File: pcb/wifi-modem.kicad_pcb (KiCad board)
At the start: 2 copper layers, 102.5 x 66.1 mm, 36 parts, among them J1 UART1 3V3 TTL, J2 RS232 DB9, J3 5.5X2.1MM, U1 74HC245, U2 WeMos_D1_mini, U3 MAX232, U4 SN74HC08N

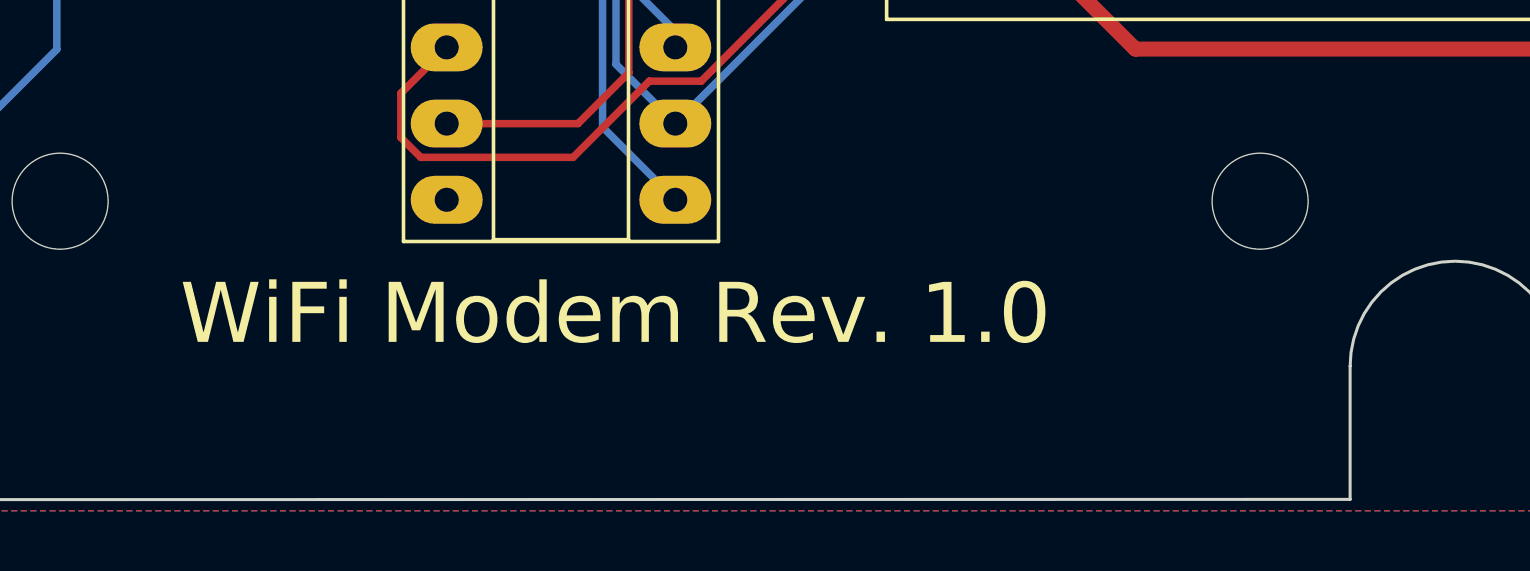
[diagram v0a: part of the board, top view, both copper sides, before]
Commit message: Rev 1.1
* Cleaning up schematic
* Adding missing copper void
* Added net names for RS232 signals
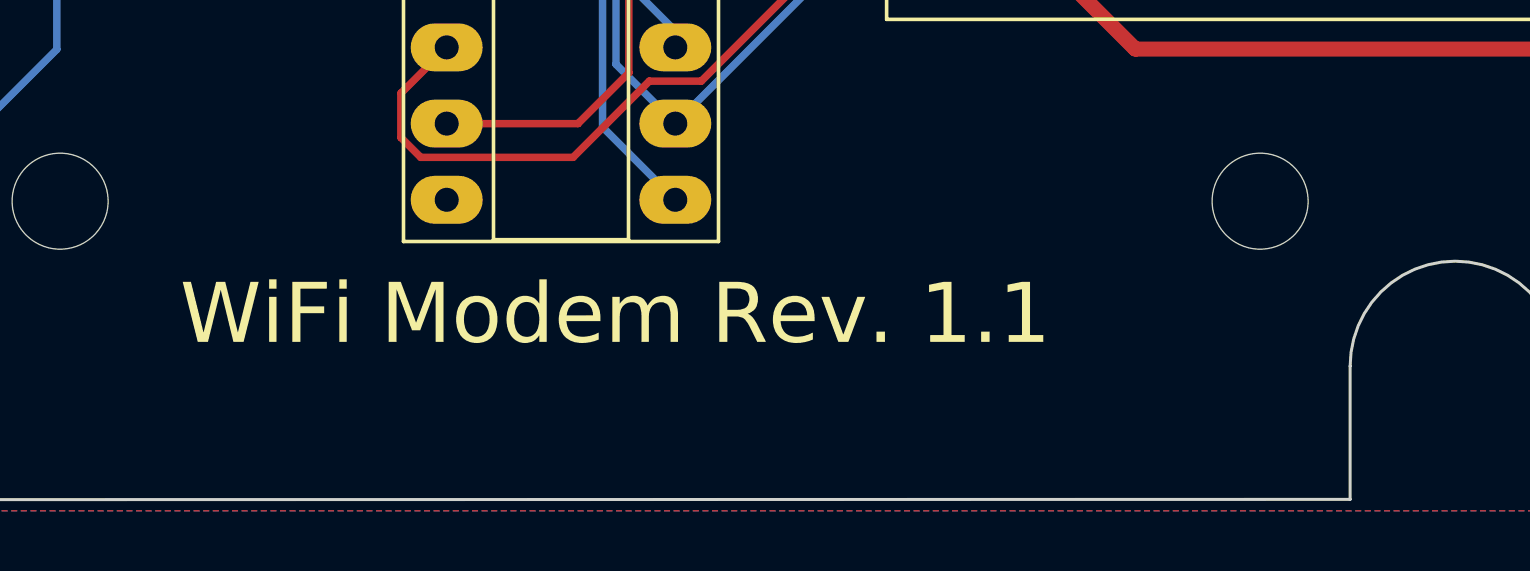
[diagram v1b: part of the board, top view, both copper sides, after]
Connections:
- net Net-(J2-Pad2) renamed /RS232_RXD
- net Net-(J2-Pad3) renamed /RS232_TXD
- net Net-(J2-Pad7) renamed /RS232_RTS
- net Net-(J2-Pad8) renamed /RS232_CTS
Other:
- board text added: "WiFi Modem Rev. 1.1"
- board text removed: "WiFi Modem Rev. 1.0"

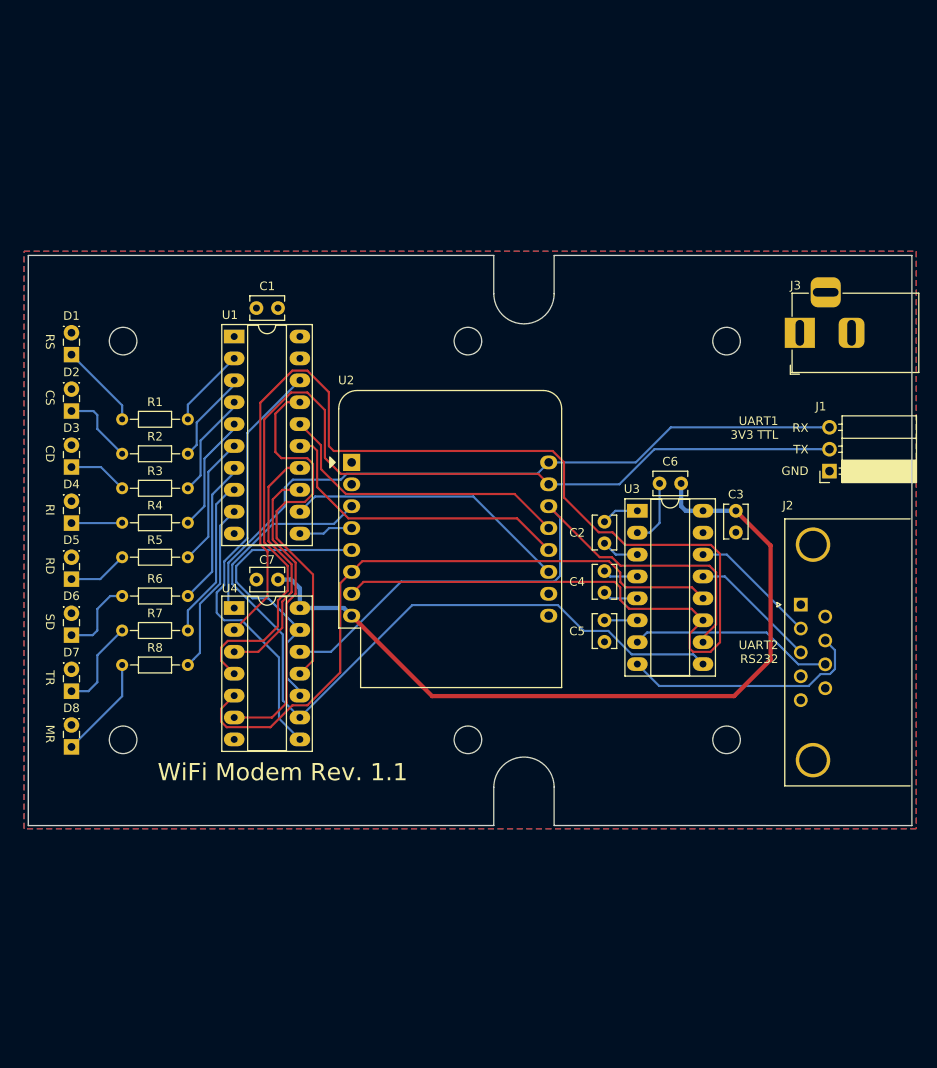
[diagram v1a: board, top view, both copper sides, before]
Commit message: PCB layout + footprint changes
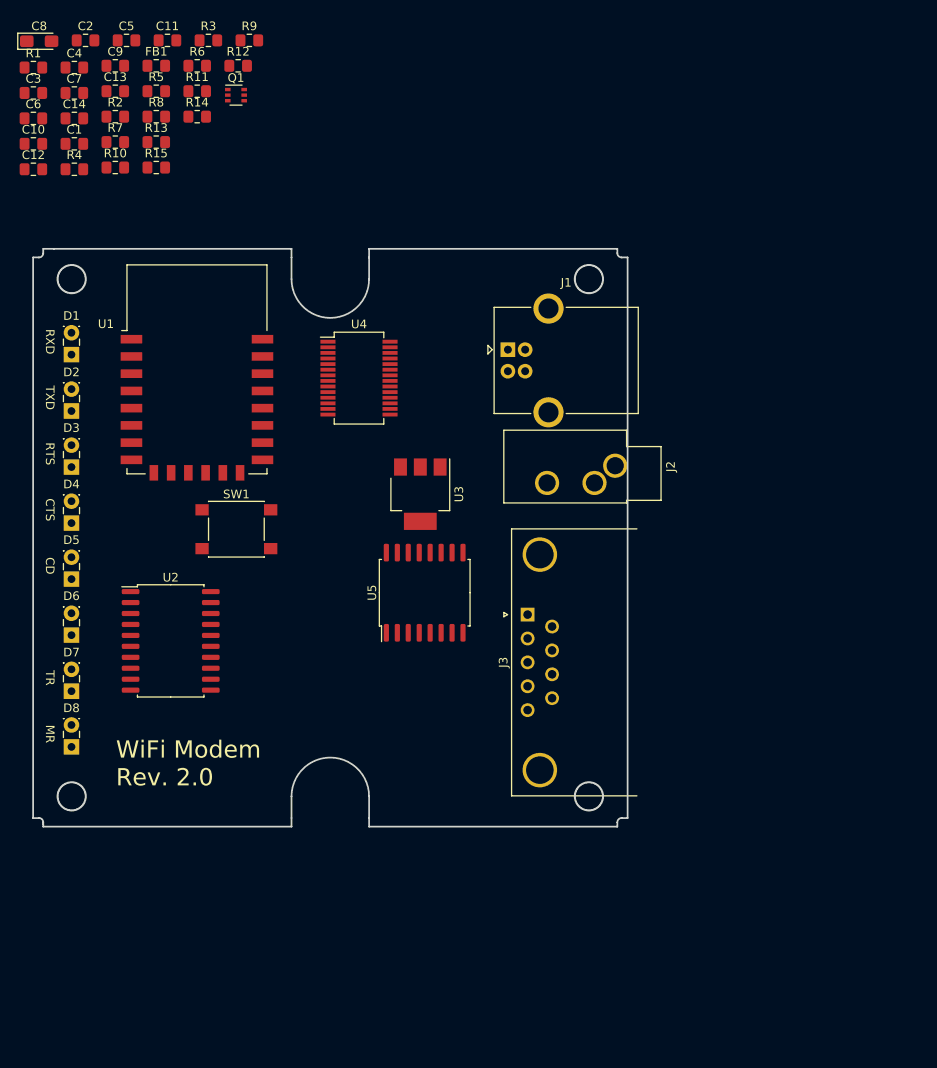
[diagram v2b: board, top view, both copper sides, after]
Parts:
- removed H5, H6: MountingHole, MountingHole:MountingHole_3.2mm_M3
- added C10: 100n, Capacitor_SMD:C_0805_2012Metric_Pad1.15x1.40mm_HandSolder, F.Cu at (38.7, 50.5)
- added C11: 100n, Capacitor_SMD:C_0805_2012Metric_Pad1.15x1.40mm_HandSolder, F.Cu at (54.2, 38.5)
- added C12: 100n, Capacitor_SMD:C_0805_2012Metric_Pad1.15x1.40mm_HandSolder, F.Cu at (38.7, 53.5)
- added C13: 100n, Capacitor_SMD:C_0805_2012Metric_Pad1.15x1.40mm_HandSolder, F.Cu at (48.2, 44.4)
- added C14: 10n, Capacitor_SMD:C_0805_2012Metric_Pad1.15x1.40mm_HandSolder, F.Cu at (43.4, 47.6)
- added C8: 4.7u, Capacitor_Tantalum_SMD:CP_EIA-3216-18_Kemet-A_Pad1.58x1.35mm_HandSolder, F.Cu at (39.4, 38.6)
- added C9: 100n, Capacitor_SMD:C_0805_2012Metric_Pad1.15x1.40mm_HandSolder, F.Cu at (48.2, 41.5)
- added FB1: 33 Ohms @ 100MHz, Inductor_SMD:L_0805_2012Metric_Pad1.15x1.40mm_HandSolder, F.Cu at (52.9, 41.5)
- added Q1: BC846BDW1, Package_TO_SOT_SMD:SOT-363_SC-70-6, F.Cu at (62.2, 44.9)
- added R10: 560, Resistor_SMD:R_0805_2012Metric_Pad1.15x1.40mm_HandSolder, F.Cu at (48.2, 53.3)
- added R11: 560, Resistor_SMD:R_0805_2012Metric_Pad1.15x1.40mm_HandSolder, F.Cu at (57.7, 44.4)
- added R12: 10k, Resistor_SMD:R_0805_2012Metric_Pad1.15x1.40mm_HandSolder, F.Cu at (62.4, 41.5)
- added R13: 10k, Resistor_SMD:R_0805_2012Metric_Pad1.15x1.40mm_HandSolder, F.Cu at (52.9, 50.3)
- added R14: 10k, Resistor_SMD:R_0805_2012Metric_Pad1.15x1.40mm_HandSolder, F.Cu at (57.7, 47.4)
- added R15: 10k, Resistor_SMD:R_0805_2012Metric_Pad1.15x1.40mm_HandSolder, F.Cu at (52.9, 53.3)
- added R9: 560, Resistor_SMD:R_0805_2012Metric_Pad1.15x1.40mm_HandSolder, F.Cu at (63.7, 38.5)
- added SW1: SW_Push, Button_Switch_SMD:SW_SPST_PTS645, F.Cu at (62.2, 95.2)
- added U5: MAX232, Package_SO:SOIC-16W_7.5x10.3mm_P1.27mm, F.Cu at (84.1, 102.6)
- C1, C2, C5, C6, C7: footprint Capacitor_THT:C_Disc_D3.8mm_W2.6mm_P2.50mm -> Capacitor_SMD:C_0805_2012Metric_Pad1.15x1.40mm_HandSolder
- C3: value 100n -> 100u; footprint Capacitor_THT:C_Disc_D3.8mm_W2.6mm_P2.50mm -> Capacitor_SMD:C_0805_2012Metric_Pad1.15x1.40mm_HandSolder
- C4: value 100n -> 10u; footprint Capacitor_THT:C_Disc_D3.8mm_W2.6mm_P2.50mm -> Capacitor_SMD:C_0805_2012Metric_Pad1.15x1.40mm_HandSolder
- D1: value RS (Request to Send) -> LED
- D2: value CS (Clear to Send) -> LED
- D3: value CD (Data Carrier Detect) -> LED
- D4: value RI (Ring) -> LED
- D5: value RD (Receive Data) -> LED
- D6: value SD (Send Data) -> LED
- D7: value TR (Terminal Ready) -> LED
- D8: value MR (Modem Ready) -> LED
- J1: value UART1 3V3 TTL -> USB_B; footprint Connector_PinSocket_2.54mm:PinSocket_1x03_P2.54mm_Horizontal -> Connector_USB:USB_B_OST_USB-B1HSxx_Horizontal
- J2: value RS232 DB9 -> AudioJack3; footprint Connector_Dsub:DSUB-9_Female_Horizontal_P2.77x2.84mm_EdgePinOffset9.90mm_Housed_MountingHolesOffset11.32mm -> Connector_Audio:Jack_3.5mm_CUI_SJ1-3533NG_Horizontal_CircularHoles
- J3: value 5.5X2.1MM -> RS232 DB9; footprint Connector_BarrelJack:BarrelJack_Horizontal -> Connector_Dsub:DSUB-9_Female_Horizontal_P2.77x2.84mm_EdgePinOffset9.90mm_Housed_MountingHolesOffset11.32mm
- R1, R2, R3: value 560 -> 10k; footprint Resistor_THT:R_Axial_DIN0204_L3.6mm_D1.6mm_P7.62mm_Horizontal -> Resistor_SMD:R_0805_2012Metric_Pad1.15x1.40mm_HandSolder
- R4, R5, R6, R7, R8: footprint Resistor_THT:R_Axial_DIN0204_L3.6mm_D1.6mm_P7.62mm_Horizontal -> Resistor_SMD:R_0805_2012Metric_Pad1.15x1.40mm_HandSolder
- U1: value 74HC245 -> ESP-12F; footprint Package_DIP:DIP-20_W7.62mm_Socket_LongPads -> RF_Module:ESP-12E
- U2: value WeMos_D1_mini -> 74HC245; footprint Module:WEMOS_D1_mini_light -> Package_SO:SOIC-20W_7.5x12.8mm_P1.27mm
- U3: value MAX232 -> LM1117-3.3; footprint Package_DIP:DIP-16_W7.62mm_Socket_LongPads -> Package_TO_SOT_SMD:SOT-223-3_TabPin2
- U4: value SN74HC08N -> FT232RL; footprint Package_DIP:DIP-14_W7.62mm_Socket_LongPads -> Package_SO:SSOP-28_5.3x10.2mm_P0.65mm
- moved C3 94.8 mm to (38.7, 44.6), turned to 0 degrees
- moved C5 87.2 mm to (49.5, 38.5), turned to 0 degrees
- moved C6 86.2 mm to (38.7, 47.6), turned to 0 degrees
- moved C4 84.8 mm to (43.4, 41.7), turned to 0 degrees
- moved C2 82.1 mm to (44.7, 38.5), turned to 0 degrees
- moved H2 76.0 mm to (103.1, 66.2)
- moved H3 70.0 mm to (43.1, 126.2)
- moved R8 63.7 mm to (52.9, 47.4), turned to 0 degrees
- moved R6 61.5 mm to (57.7, 41.5), turned to 0 degrees
- moved C7 61.2 mm to (43.4, 44.6), turned to 0 degrees
- moved R7 57.3 mm to (48.2, 50.3), turned to 0 degrees
- moved R5 54.2 mm to (52.9, 44.4), turned to 0 degrees
- moved R3 52.0 mm to (59.0, 38.5), turned to 0 degrees
- moved J3 45.4 mm to (96.0, 105.2), turned to 90 degrees
- moved R1 44.6 mm to (38.7, 41.7), turned to 0 degrees
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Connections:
- C2 pad 1: Net-(C2-Pad1) -> +3V3
- C2 pad 2: Net-(C2-Pad2) -> GND
- C4 pad 1: Net-(C4-Pad1) -> +5V
- C4 pad 2: Net-(C4-Pad2) -> GND
- C5 pad 1: Net-(C5-Pad1) -> +5V
- C6 pad 1: +3V3 -> Net-(C6-Pad1)
- J1 pad 1: GND -> VBUS
- J1 pad 2: TX1 -> Net-(J1-Pad2)
- J1 pad 3: RX1 -> Net-(J1-Pad3)
- J3 pad 1: +5V -> (no net)
- J3 pad 2: GND -> RS232_TXD
- J3 pad 3: Net-(J3-Pad3) -> RS232_RXD
- R1 pad 1: Net-(R1-Pad1) -> +3V3
- R1 pad 2: Net-(D1-Pad1) -> ESP_GPIO2
- R2 pad 1: Net-(R2-Pad1) -> +3V3
- R2 pad 2: Net-(D2-Pad1) -> ESP_GPIO0
- R3 pad 1: Net-(R3-Pad1) -> +3V3
- R3 pad 2: Net-(D3-Pad1) -> ESP_RST_N
- R4 pad 1: Net-(R4-Pad1) -> RX_LED_DRV
- R4 pad 2: Net-(D4-Pad1) -> Net-(D1-Pad1)
- R5 pad 1: Net-(R5-Pad1) -> TX_LED_DRV
- R5 pad 2: Net-(D5-Pad1) -> Net-(D2-Pad1)
- R6 pad 1: Net-(R6-Pad1) -> RTS_LED_DRV
- R6 pad 2: Net-(D6-Pad1) -> Net-(D3-Pad1)
- R7 pad 1: Net-(R7-Pad1) -> CTS_LED_DRV
- R7 pad 2: Net-(D7-Pad1) -> Net-(D4-Pad1)
- R8 pad 1: Net-(R8-Pad1) -> CD_LED_DRV
- R8 pad 2: Net-(D8-Pad1) -> Net-(D5-Pad1)
- U1 pad 1: GND -> ESP_RST_N
- U1 pad 10: GND -> (no net)
- U1 pad 11: MR -> (no net)
- U1 pad 12: TR -> (no net)
- U1 pad 13: TX_LED -> (no net)
- U1 pad 14: RX_LED -> (no net)
- U1 pad 15: RI -> GND
- U1 pad 16: CD -> ESP_GPIO15_UART0_RTS
- U1 pad 17: CS_LED -> ESP_GPIO2
- U1 pad 18: RS_LED -> ESP_GPIO0
- U1 pad 19: GND -> ESP_GPIO4
- U1 pad 2: Net-(R1-Pad1) -> (no net)
- U1 pad 20: +5V -> ESP_GPIO5
- U1 pad 3: Net-(R2-Pad1) -> ESP_EN
- U1 pad 4: Net-(R3-Pad1) -> (no net)
- U1 pad 5: Net-(R4-Pad1) -> ESP_GPIO14
- U1 pad 6: Net-(R5-Pad1) -> ESP_GPIO12
- U1 pad 7: Net-(R6-Pad1) -> ESP_UART0_CTS
- U1 pad 8: Net-(R7-Pad1) -> +3V3
- U1 pad 9: Net-(R8-Pad1) -> (no net)
- U2 pad 1: Net-(U2-Pad1) -> GND
- U2 pad 11: TR -> ESP_GPIO14
- U2 pad 12: RI -> ESP_GPIO12
- U2 pad 13: CD -> ESP_GPIO5
- U2 pad 14: CS -> ESP_GPIO4
- U2 pad 15: TX1 -> ESP_GPIO15_UART0_RTS
- U2 pad 16: RX1 -> ESP_UART0_CTS
- U2 pad 2: Net-(U2-Pad2) -> RX_LED_DRV
- U2 pad 3: RS -> TX_LED_DRV
- U2 pad 4: MR -> RTS_LED_DRV
- U2 pad 5: HS_DISP_CTRL -> CTS_LED_DRV
- U2 pad 6: TX2 -> CD_LED_DRV
- U2 pad 7: RX2 -> RI_LED_DRV
- U2 pad 8: +3V3 -> TR_LED_DRV
- U2 pad 9: +5V -> MR_LED_DRV
- U3 pad 1: Net-(C2-Pad1) -> GND
- U3 pad 2: Net-(C6-Pad2) -> +3V3
- U3 pad 3: Net-(C2-Pad2) -> +5V
- U4 pad 1: RX1 -> 3V3_TTL_RXD
- U4 pad 10: HS_DISP_CTRL -> (no net)
- U4 pad 11: CS_LED -> ESP_GPIO15_UART0_RTS
- U4 pad 12: CS -> (no net)
- U4 pad 13: HS_DISP_CTRL -> (no net)
- U4 pad 14: +3V3 -> (no net)
- U4 pad 2: RX2 -> FT232_DTR
- U4 pad 3: RX_LED -> ESP_UART0_CTS
- U4 pad 4: TX1 -> FT232_3V3
- U4 pad 5: TX2 -> 3V3_TTL_TXD
- U4 pad 6: TX_LED -> (no net)
- U4 pad 8: RS_LED -> (no net)
- U4 pad 9: RS -> (no net)
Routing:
- net RX2: track 160.4 -> 0.00 mm
- net TX1: track 113.1 -> 0.00 mm
- net +3V3: track 94.0 -> 0.00 mm
- net RS: track 92.7 -> 0.00 mm
- net RX1: track 83.0 -> 0.00 mm
- net TX2: track 76.3 -> 0.00 mm
- net CS: track 73.8 -> 0.00 mm
- net RS_LED: track 50.8 -> 0.00 mm
- net CS_LED: track 42.6 -> 0.00 mm
- net RI: track 36.3 -> 0.00 mm
- net TX_LED: track 35.5 -> 0.00 mm
- net CD: track 35.5 -> 0.00 mm
- net HS_DISP_CTRL: track 34.6 -> 0.00 mm
- net TR: track 33.2 -> 0.00 mm
- net RX_LED: track 29.2 -> 0.00 mm
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- removed copper zone on B.Cu, net +5V
- removed copper zone on F.Cu, net GND
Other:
- board size 102.5 x 66.1 mm -> 69 x 67 mm
- board text added: "CTS"
- board text added: "RTS"
- board text added: "RXD"
- board text added: "TXD"
- board text added: "WiFi Modem Rev. 2.0"
- board text removed: "CS"
- board text removed: "GND"
- board text removed: "RD"
- board text removed: "RI"
- board text removed: "RS"
- board text removed: "RX"
- board text removed: "SD"
- board text removed: "TX"
- board text removed: "UART1 3V3 TTL"
- board text removed: "UART2 RS232"
- board text removed: "WiFi Modem Rev. 1.1"

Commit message: Added 100nF cap between RST_N and GND and additional 10uF cap near 3.3V rail of ESP module
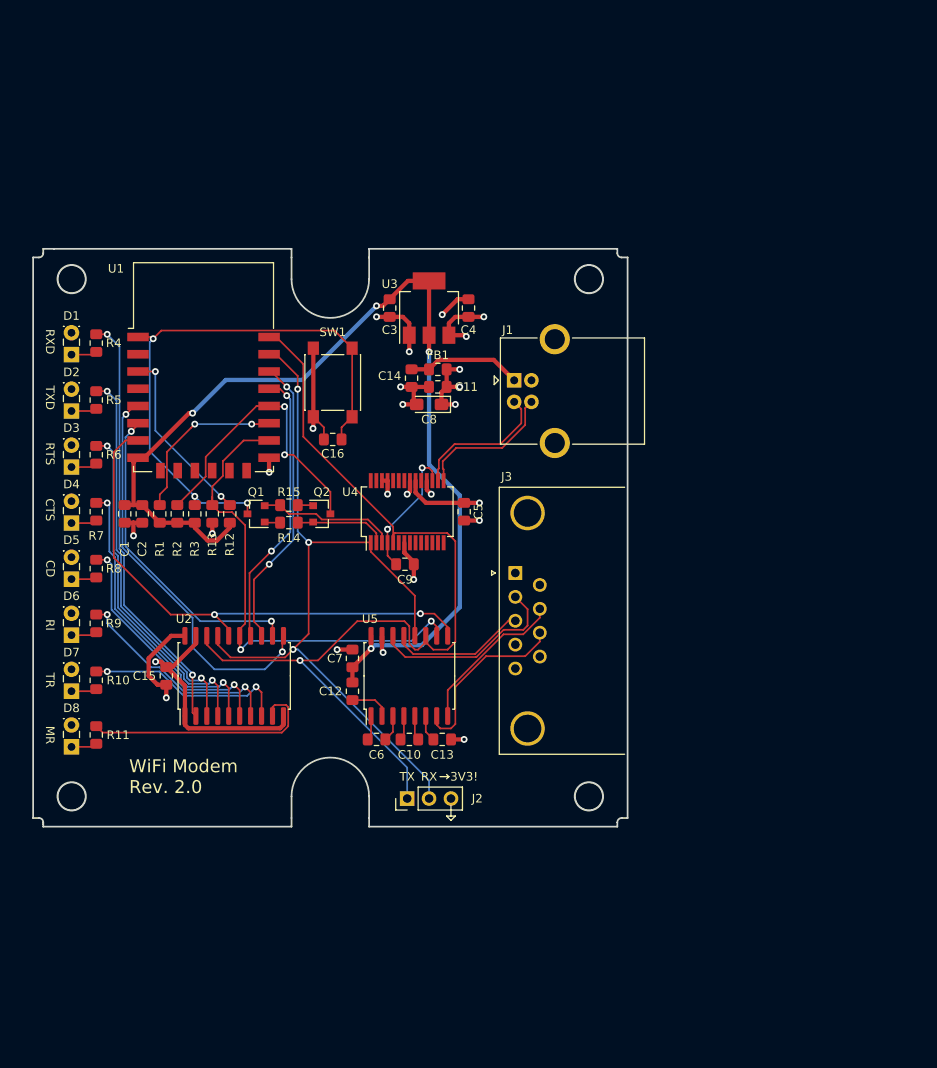
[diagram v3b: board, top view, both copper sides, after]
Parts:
- added C1: 10u, Capacitor_SMD:C_0805_2012Metric_Pad1.15x1.40mm_HandSolder, F.Cu at (49.3, 93.5)
- added C16: 100n, Capacitor_SMD:C_0805_2012Metric_Pad1.15x1.40mm_HandSolder, F.Cu at (73.4, 84.8)
- added Q2: Q_NPN_BEC, Package_TO_SOT_SMD:SOT-23, F.Cu at (72.1, 93.5)
- J2: value AudioJack3 -> Conn_01x03; footprint Connector_Audio:Jack_3.5mm_CUI_SJ1-3533NG_Horizontal_CircularHoles -> Connector_PinHeader_2.54mm:PinHeader_1x03_P2.54mm_Vertical
- Q1: value BC846BDW1 -> Q_NPN_BEC; footprint Package_TO_SOT_SMD:SOT-363_SC-70-6 -> Package_TO_SOT_SMD:SOT-23
- moved C13 84.2 mm to (86.1, 119.6)
- moved C6 82.3 mm to (78.5, 119.6)
- moved C10 81.7 mm to (82.3, 119.6)
- moved R11 75.6 mm to (46.0, 119.1), turned to 270 degrees
- moved C7 73.1 mm to (75.7, 110.2), turned to 90 degrees
- moved C12 71.0 mm to (75.7, 114.0), turned to 270 degrees
- moved R9 69.9 mm to (46.0, 106.2), turned to 270 degrees
- moved C5 67.3 mm to (88.6, 93.2), turned to 270 degrees
- moved C9 66.9 mm to (81.8, 99.3)
- moved C15 62.6 mm to (54.1, 112.3), turned to 90 degrees
- moved C8 61.8 mm to (84.6, 80.8), turned to 180 degrees
- moved R10 59.5 mm to (46.0, 112.8), turned to 270 degrees
- moved C2 55.3 mm to (51.3, 93.5), turned to 270 degrees
- moved R3 54.9 mm to (57.4, 93.5), turned to 90 degrees
- moved R1 53.8 mm to (53.3, 93.5), turned to 90 degrees
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- renumbered C1 to C15
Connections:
- net Net-(J1-Pad2) renamed FT232_USBD-
- net Net-(J1-Pad3) renamed FT232_USBD+
- Q1 pad 1: FT232_DTR -> Net-(Q1-Pad1)
- Q1 pad 2: Net-(Q1-Pad2) -> FT232_RTS
- R14 pad 1: Net-(Q1-Pad5) -> Net-(Q1-Pad1)
- R15 pad 1: Net-(Q1-Pad2) -> Net-(Q2-Pad1)
- R15 pad 2: ESP_UART0_CTS -> FT232_RTS
- U4 pad 11: ESP_GPIO15_UART0_RTS -> (no net)
- U4 pad 3: ESP_UART0_CTS -> FT232_RTS
- U5 pad 10: ESP_UART0_CTS -> ESP_GPIO15_UART0_RTS
- U5 pad 11: 3V3_TTL_RXD -> 3V3_TTL_TXD
- U5 pad 12: 3V3_TTL_TXD -> 3V3_TTL_RXD
- U5 pad 9: ESP_GPIO15_UART0_RTS -> ESP_UART0_CTS
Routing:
- net +3V3: track 0.00 -> 121.3 mm, vias 0 -> 4
- net 3V3_TTL_TXD: track 0.00 -> 109.4 mm, vias 0 -> 1
- net 3V3_TTL_RXD: track 0.00 -> 92.4 mm, vias 0 -> 3
- net GND: track 0.00 -> 82.1 mm, vias 0 -> 18
- net ESP_RST_N: track 0.00 -> 66.6 mm, vias 0 -> 3
- net ESP_UART0_CTS: track 0.00 -> 61.9 mm, vias 0 -> 2
- net ESP_GPIO15_UART0_RTS: track 0.00 -> 57.9 mm, vias 0 -> 2
- net RX_LED_DRV: track 0.00 -> 49.8 mm, vias 0 -> 2
- net ESP_GPIO14: track 0.00 -> 46.6 mm, vias 0 -> 2
- net TX_LED_DRV: track 0.00 -> 44.9 mm, vias 0 -> 2
- net RTS_LED_DRV: track 0.00 -> 40.1 mm, vias 0 -> 2
- net +5V: track 0.00 -> 37.4 mm, vias 0 -> 7
- net ESP_GPIO12: track 0.00 -> 37.2 mm, vias 0 -> 2
- net CTS_LED_DRV: track 0.00 -> 35.0 mm, vias 0 -> 2
- net ESP_GPIO5: track 0.00 -> 34.2 mm, vias 0 -> 2
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- added copper zone on In2.Cu, net +5V
- added copper zone on In1.Cu, net GND
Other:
- copper layers 2 -> 4
- net class Default: clearance 0.2 -> 0.15; trace_width 0.25 -> 0.2
- net class Power: clearance 0.2 -> 0.15
- rule pad_to_mask_clearance: 0.05 -> 0.0508
- rule trace_clearance: 0.2 -> 0.15
- rule trace_min: 0.2 -> 0.127
- rule via_min_drill: 0.3 -> 0.254
- rule via_min_size: 0.4 -> 0.4572
- board text added: "3V3!"
- board text added: "RI"
- board text added: "RX"
- board text added: "TX"
